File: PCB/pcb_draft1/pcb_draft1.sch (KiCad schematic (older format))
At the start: 76 parts, among them J1 Screw_Terminal_01x03, J2 12V_Power A97996-ND, J3 HomeSwitch, J4 Therm1, J5 ArdAnalogTherm, J6 Therm2, Q1 DMN6140L, Q10 DMN6140L, Q11 DMN6140L, Q12 DMN6140L, Q13 DMN6140L, Q14 DMN6140L, Q15 DMN6140L, Q2 DMN6140L, Q3 DMN6140L, Q4 DMN6140L, Q5 DMN6140L, Q6 DMN6140L, Q7 DMN6140L, Q8 DMN6140L, Q9 DMN6140L, U1 STSPIN820, U2 STSPIN820, Y1 Arduino_Mega_Bottom_Pins1

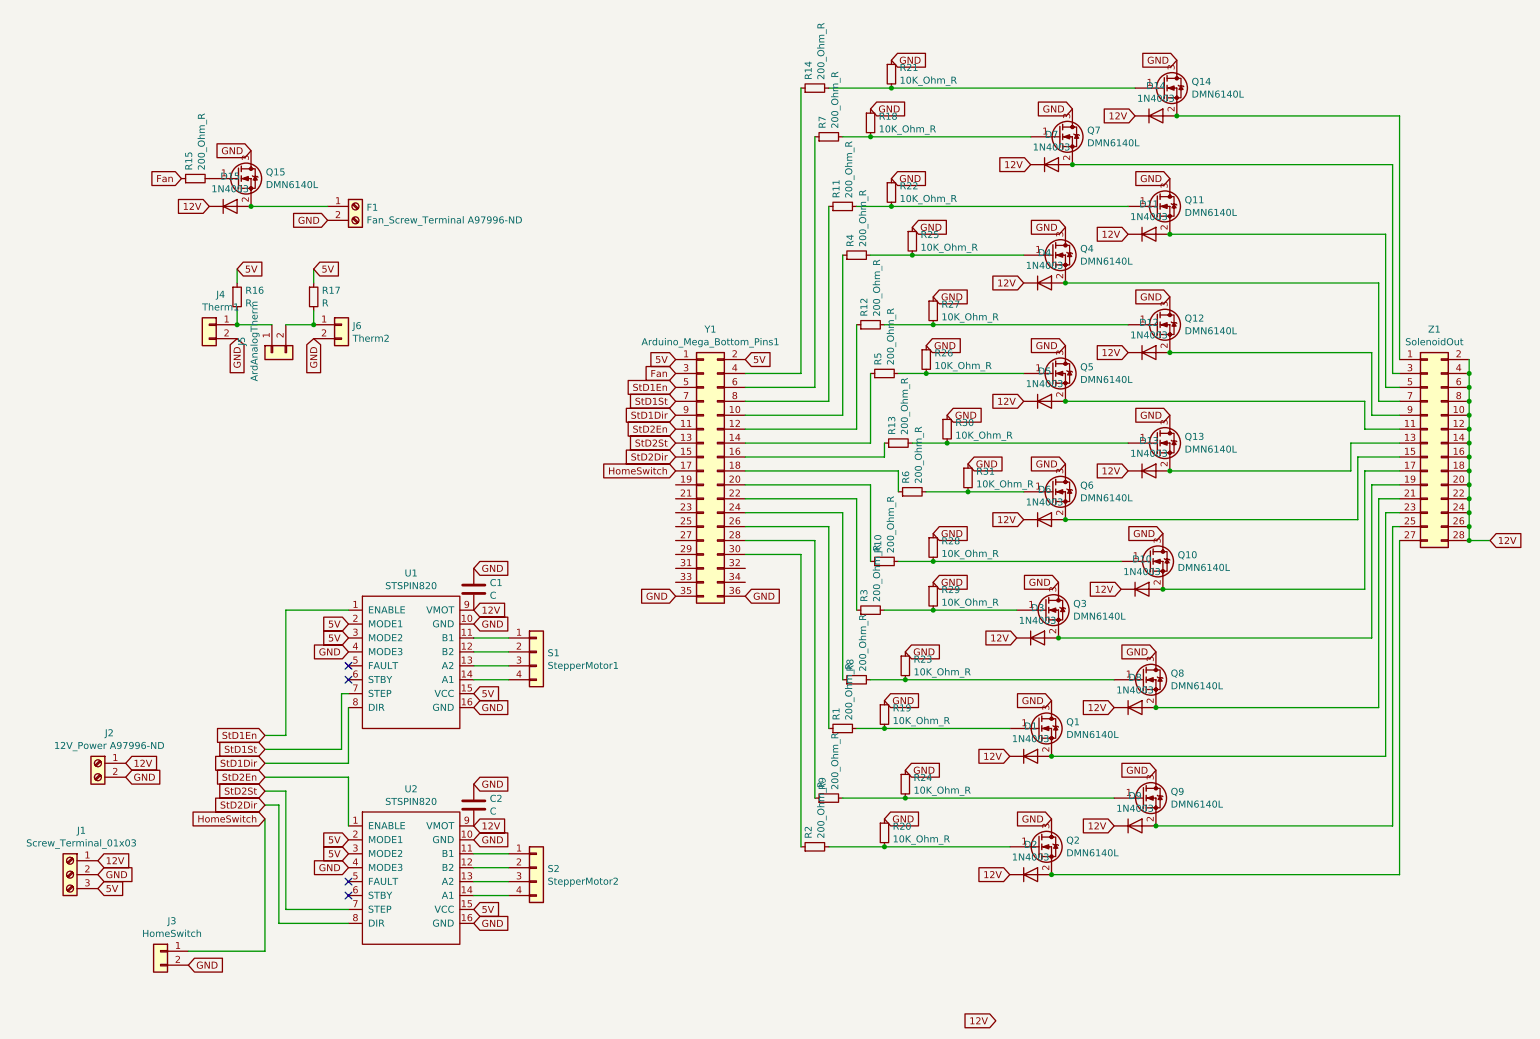
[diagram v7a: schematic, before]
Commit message: Add footprints and finalize layout - need to add 10kohm resistors
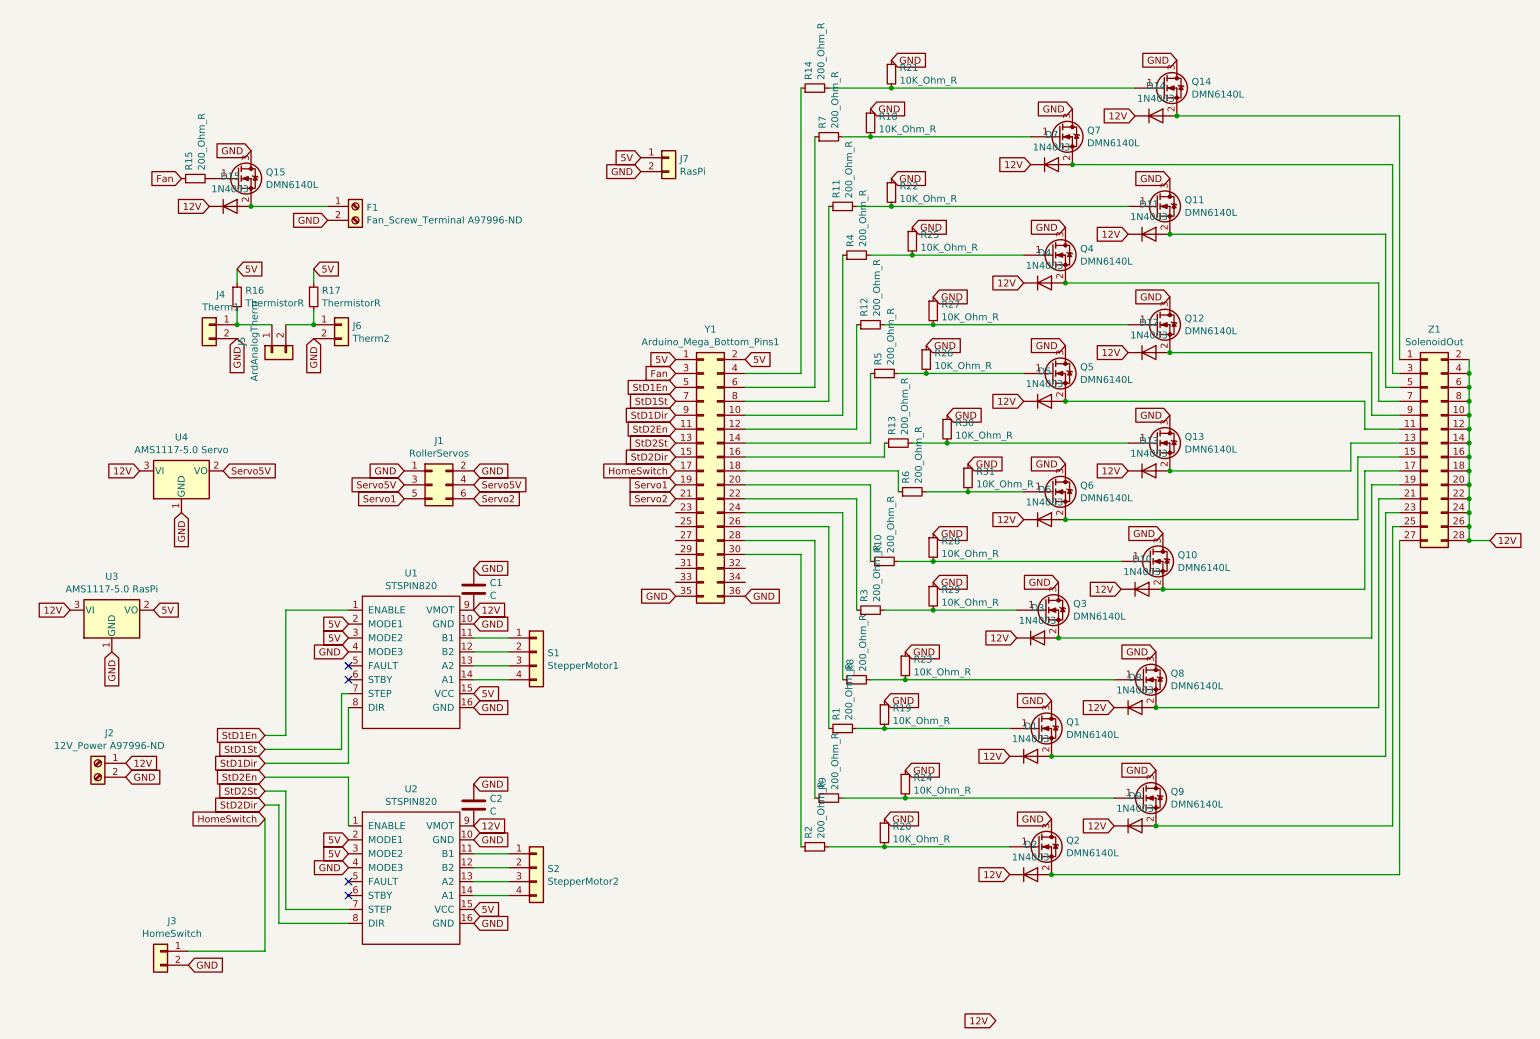
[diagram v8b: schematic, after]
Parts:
- removed J1: Screw_Terminal_01x03, symbol Connector:Screw_Terminal_01x03
- added J1: RollerServos, Connector_PinHeader_2.54mm:PinHeader_2x03_P2.54mm_Vertical, symbol Connector_Generic:Conn_02x03_Odd_Even
- added J7: RasPi, Connector_PinHeader_2.54mm:PinHeader_1x02_P2.54mm_Vertical, symbol Connector_Generic:Conn_01x02
- added U3: AMS1117-5.0 RasPi, Package_TO_SOT_SMD:SOT-223-3_TabPin2, symbol Regulator_Linear:AMS1117-5.0
- added U4: AMS1117-5.0 Servo, Package_TO_SOT_SMD:SOT-223-3_TabPin2, symbol Regulator_Linear:AMS1117-5.0
- C1, C2: footprint Capacitor_SMD:C_1206_3216Metric -> Capacitor_THT:CP_Radial_D8.0mm_P3.50mm
- J2: footprint (none) -> TerminalBlock_Phoenix:TerminalBlock_Phoenix_MKDS-1,5-2_1x02_P5.00mm_Horizontal
- J3, J4, J5, J6: footprint (none) -> Connector_PinHeader_2.54mm:PinHeader_1x02_P2.54mm_Vertical
- R16, R17: value R -> ThermistorR; footprint (none) -> Connector_PinHeader_2.54mm:PinHeader_1x02_P2.54mm_Vertical
- S1, S2: footprint (none) -> Connector_PinHeader_2.54mm:PinHeader_1x04_P2.54mm_Vertical
- Y1: footprint (none) -> Connector_PinHeader_2.54mm:PinHeader_2x18_P2.54mm_Vertical
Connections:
- net 12V: now also U3.3 (VI), U4.3 (VI)
- net 5V: now also J7.1 (Pin_1), U3.2 (VO)
- net GND: now also J1.1 (Pin_1), J1.2 (Pin_2), J7.2 (Pin_2), U3.1 (GND), U4.1 (GND)
- net Servo1: now reaches Y1.19 (Pin_19)
- net Servo1: now also J1.5 (Pin_5)
- net Servo2: now reaches Y1.21 (Pin_21)
- net Servo2: now also J1.6 (Pin_6)
- new net Servo5V: J1.3 (Pin_3), J1.4 (Pin_4), U4.2 (VO)
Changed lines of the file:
@@
 Text GLabel 1300 5750 2    50   Input ~ 0
-GND
-Text GLabel 1100 6350 2    50   Input ~ 0
-12V
-Text GLabel 1100 6450 2    50   Input ~ 0
 GND
 Text GLabel 8850 600  0    50   Input ~ 0
@@
 Text GLabel 3800 6700 2    50   Input ~ 0
 5V
-Text GLabel 1100 6550 2    50   Input ~ 0
-5V
 Text GLabel 3800 4550 2    50   Input ~ 0
 12V
@@
 F 0 "C2" H 3915 5996 50  0000 L CNN
 F 1 "C" H 3915 5905 50  0000 L CNN
-F 2 "Capacitor_SMD:C_1206_3216Metric" H 3838 5800 50  0001 C CNN
+F 2 "Capacitor_THT:CP_Radial_D8.0mm_P3.50mm" H 3838 5800 50  0001 C CNN
 F 3 "~" H 3800 5950 50  0001 C CNN
 	1    3800 5950
@@
 F 0 "C1" H 3915 4446 50  0000 L CNN
 F 1 "C" H 3915 4355 50  0000 L CNN
-F 2 "Capacitor_SMD:C_1206_3216Metric" H 3838 4250 50  0001 C CNN
+F 2 "Capacitor_THT:CP_Radial_D8.0mm_P3.50mm" H 3838 4250 50  0001 C CNN
 F 3 "~" H 3800 4400 50  0001 C CNN
 	1    3800 4400
@@
 P 2100 2300
 F 0 "R16" H 2159 2346 50  0000 L CNN
-F 1 "R" H 2159 2255 50  0000 L CNN
-F 2 "" H 2100 2300 50  0001 C CNN
+F 1 "ThermistorR" H 2159 2255 50  0000 L CNN
+F 2 "Connector_PinHeader_2.54mm:PinHeader_1x02_P2.54mm_Vertical" H 2100 2300 50  0001 C CNN
 F 3 "~" H 2100 2300 50  0001 C CNN
 	1    2100 2300
@@
 P 2650 2300
 F 0 "R17" H 2709 2346 50  0000 L CNN
-F 1 "R" H 2709 2255 50  0000 L CNN
-F 2 "" H 2650 2300 50  0001 C CNN
+F 1 "ThermistorR" H 2709 2255 50  0000 L CNN
+F 2 "Connector_PinHeader_2.54mm:PinHeader_1x02_P2.54mm_Vertical" H 2650 2300 50  0001 C CNN
 F 3 "~" H 2650 2300 50  0001 C CNN
 	1    2650 2300
@@
 F 0 "Y1" H 5500 4567 50  0000 C CNN
 F 1 "Arduino_Mega_Bottom_Pins1" H 5500 4476 50  0000 C CNN
-F 2 "" H 5450 3550 50  0001 C CNN
+F 2 "Connector_PinHeader_2.54mm:PinHeader_2x18_P2.54mm_Vertical" H 5450 3550 50  0001 C CNN
 F 3 "~" H 5450 3550 50  0001 C CNN
 	1    5450 3550
@@
 F 0 "S2" H 4330 6392 50  0000 L CNN
 F 1 "StepperMotor2" H 4330 6301 50  0000 L CNN
-F 2 "" H 4250 6400 50  0001 C CNN
+F 2 "Connector_PinHeader_2.54mm:PinHeader_1x04_P2.54mm_Vertical" H 4250 6400 50  0001 C CNN
 F 3 "~" H 4250 6400 50  0001 C CNN
 	1    4250 6400
@@
 F 0 "S1" H 4330 4842 50  0000 L CNN
 F 1 "StepperMotor1" H 4330 4751 50  0000 L CNN
-F 2 "" H 4250 4850 50  0001 C CNN
+F 2 "Connector_PinHeader_2.54mm:PinHeader_1x04_P2.54mm_Vertical" H 4250 4850 50  0001 C CNN
 F 3 "~" H 4250 4850 50  0001 C CNN
 	1    4250 4850
@@
 F 0 "J5" H 2268 2917 50  0000 C CNN
 F 1 "ArdAnalogTherm" H 2268 2826 50  0000 C CNN
-F 2 "" H 2350 2700 50  0001 C CNN
+F 2 "Connector_PinHeader_2.54mm:PinHeader_1x02_P2.54mm_Vertical" H 2350 2700 50  0001 C CNN
 F 3 "~" H 2350 2700 50  0001 C CNN
 	1    2350 2700
@@
 F 0 "J4" H 1818 2717 50  0000 C CNN
 F 1 "Therm1" H 1818 2626 50  0000 C CNN
-F 2 "" H 1900 2500 50  0001 C CNN
+F 2 "Connector_PinHeader_2.54mm:PinHeader_1x02_P2.54mm_Vertical" H 1900 2500 50  0001 C CNN
 F 3 "~" H 1900 2500 50  0001 C CNN
 	1    1900 2500
@@
 F 0 "J6" H 2930 2492 50  0000 L CNN
 F 1 "Therm2" H 2930 2401 50  0000 L CNN
-F 2 "" H 2850 2500 50  0001 C CNN
+F 2 "Connector_PinHeader_2.54mm:PinHeader_1x02_P2.54mm_Vertical" H 2850 2500 50  0001 C CNN
 F 3 "~" H 2850 2500 50  0001 C CNN
 	1    2850 2500
@@
 F 0 "J3" H 1468 7217 50  0000 C CNN
 F 1 "HomeSwitch" H 1468 7126 50  0000 C CNN
-F 2 "" H 1550 7000 50  0001 C CNN
+F 2 "Connector_PinHeader_2.54mm:PinHeader_1x02_P2.54mm_Vertical" H 1550 7000 50  0001 C CNN
 F 3 "~" H 1550 7000 50  0001 C CNN
 	1    1550 7000
-	-1   0    0    -1
-$EndComp
-$Comp
-L Connector:Screw_Terminal_01x03 J1
-U 1 1 5E155D7D
-P 900 6450
-F 0 "J1" H 818 6767 50  0000 C CNN
-F 1 "Screw_Terminal_01x03" H 818 6676 50  0000 C CNN
-F 2 "" H 900 6450 50  0001 C CNN
-F 3 "~" H 900 6450 50  0001 C CNN
-	1    900  6450
 	-1   0    0    -1
 $EndComp
@@
 F 0 "J2" H 1018 5867 50  0000 C CNN
 F 1 "12V_Power A97996-ND " H 1018 5776 50  0000 C CNN
-F 2 "" H 1100 5650 50  0001 C CNN
+F 2 "TerminalBlock_Phoenix:TerminalBlock_Phoenix_MKDS-1,5-2_1x02_P5.00mm_Horizontal" H 1100 5650 50  0001 C CNN
 F 3 "~" H 1100 5650 50  0001 C CNN
 	1    1100 5650
 	-1   0    0    -1
 $EndComp
+Text GLabel 3300 3550 0    50   Input ~ 0
+GND
+Text GLabel 3800 3550 2    50   Input ~ 0
+GND
+Text GLabel 3800 3650 2    50   Input ~ 0
+Servo5V
+Text GLabel 3300 3650 0    50   Input ~ 0
+Servo5V
+Text GLabel 3300 3750 0    50   Input ~ 0
+Servo1
+Text GLabel 5250 3750 0    50   Input ~ 0
+Servo2
+Text GLabel 3800 3750 2    50   Input ~ 0
+Servo2
+Text GLabel 5250 3650 0    50   Input ~ 0
+Servo1
+$Comp
+L Regulator_Linear:AMS1117-5.0 U4
+U 1 1 5DD0B91E
+P 1700 3550
+F 0 "U4" H 1700 3792 50  0000 C CNN
+F 1 "AMS1117-5.0 Servo" H 1700 3701 50  0000 C CNN
+F 2 "Package_TO_SOT_SMD:SOT-223-3_TabPin2" H 1700 3750 50  0001 C CNN
+F 3 "http://www.advanced-monolithic.com/pdf/ds1117.pdf" H 1800 3300 50  0001 C CNN
+	1    1700 3550
+	1    0    0    -1
+$EndComp
+Text GLabel 1400 3550 0    50   Input ~ 0
+12V
+Text GLabel 2000 3550 2    50   Input ~ 0
+Servo5V
+Text GLabel 1700 3850 3    50   Input ~ 0
+GND
+$Comp
+L Regulator_Linear:AMS1117-5.0 U3
+U 1 1 5DD2CA4F
+P 1200 4550
+F 0 "U3" H 1200 4792 50  0000 C CNN
+F 1 "AMS1117-5.0 RasPi" H 1200 4701 50  0000 C CNN
+F 2 "Package_TO_SOT_SMD:SOT-223-3_TabPin2" H 1200 4750 50  0001 C CNN
+F 3 "http://www.advanced-monolithic.com/pdf/ds1117.pdf" H 1300 4300 50  0001 C CNN
+	1    1200 4550
+	1    0    0    -1
+$EndComp
+Text GLabel 900  4550 0    50   Input ~ 0
+12V
+Text GLabel 1500 4550 2    50   Input ~ 0
+5V
+Text GLabel 1200 4850 3    50   Input ~ 0
+GND
+$Comp
+L Connector_Generic:Conn_01x02 J7
+U 1 1 5DD35823
+P 5200 1300
+F 0 "J7" H 5280 1292 50  0000 L CNN
+F 1 "RasPi" H 5280 1201 50  0000 L CNN
+F 2 "Connector_PinHeader_2.54mm:PinHeader_1x02_P2.54mm_Vertical" H 5200 1300 50  0001 C CNN
+F 3 "~" H 5200 1300 50  0001 C CNN
+	1    5200 1300
+	1    0    0    -1
+$EndComp
+Text GLabel 5000 1400 0    50   Input ~ 0
+GND
+Text GLabel 5000 1300 0    50   Input ~ 0
+5V
+$Comp
+L Connector_Generic:Conn_02x03_Odd_Even J1
+U 1 1 5DD6D984
+P 3500 3650
+F 0 "J1" H 3550 3967 50  0000 C CNN
+F 1 "RollerServos" H 3550 3876 50  0000 C CNN
+F 2 "Connector_PinHeader_2.54mm:PinHeader_2x03_P2.54mm_Vertical" H 3500 3650 50  0001 C CNN
+F 3 "~" H 3500 3650 50  0001 C CNN
+	1    3500 3650
+	1    0    0    -1
+$EndComp
 $EndSCHEMATC
